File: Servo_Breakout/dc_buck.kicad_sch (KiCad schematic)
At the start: 18 parts, among them U301 BD9G500EFJ-LAE2

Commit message: finalized schematic. footprints in progress
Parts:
- C302, C305, C307, C308, C309, C310: footprint (none) -> Capacitor_SMD:C_0603_1608Metric
- C304: footprint (none) -> Capacitor_SMD:C_0603_1608Metric; now not fitted
- C306: footprint (none) -> Capacitor_THT:CP_Radial_D16.0mm_P7.50mm
- L301: footprint (none) -> Inductor_Vishay:L_Vishay_IHLP-3232
- R301, R302, R303, R305, R306, R307: footprint (none) -> Resistor_SMD:R_0603_1608Metric
- R304: footprint (none) -> Resistor_SMD:R_0603_1608Metric; now not fitted
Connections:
- net EPAD is gone; now on net GND: U301.EPAD (EXP-PAD)
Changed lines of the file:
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@@
+	(wire
+		(pts
+			(xy 180.34 91.44) (xy 180.34 95.25)
+		)
+		(stroke
+			(width 0)
+			(type default)
+		)
+	)
 	(wire
 		(pts
@@
 	(wire
 		(pts
+			(xy 69.85 90.17) (xy 82.55 90.17)
+		)
+		(stroke
+			(width 0)
+			(type default)
+		)
+	)
+	(wire
+		(pts
 			(xy 69.85 68.58) (xy 82.55 68.58)
 		)
@@
 	(wire
 		(pts
-			(xy 82.55 90.17) (xy 69.85 90.17)
-		)
-		(stroke
-			(width 0)
-			(type default)
-		)
-	)
-	(wire
-		(pts
 			(xy 194.31 97.79) (xy 194.31 100.33)
 		)
@@
 			(width 0)
 			(type default)
-		)
-	)
-	(label "EPAD"
-		(at 180.34 95.25 0)
-		(effects
-			(font
-				(size 1.27 1.27)
-			)
-			(justify left)
 		)
 	)
@@
 		)
 	)
+	(hierarchical_label "GND"
+		(shape bidirectional)
+		(at 180.34 91.44 90)
+		(effects
+			(font
+				(size 1.27 1.27)
+			)
+			(justify left)
+		)
+	)
 	(symbol
 		(lib_id "Device:R_US")
@@
 			)
 		)
-		(property "Footprint" ""
+		(property "Footprint" "Resistor_SMD:R_0603_1608Metric"
 			(at 181.356 113.284 90)
 			(effects
@@
 			)
 		)
-		(property "Footprint" ""
+		(property "Footprint" "Capacitor_SMD:C_0603_1608Metric"
 			(at 207.9752 107.95 0)
 			(effects
@@
 		(in_bom yes)
 		(on_board yes)
-		(dnp no)
+		(dnp yes)
 		(fields_autoplaced yes)
 		(property "Reference" "R304"
@@
 			)
 		)
-		(property "Footprint" ""
+		(property "Footprint" "Resistor_SMD:R_0603_1608Metric"
 			(at 120.396 75.184 90)
 			(effects
@@
 			)
 		)
-		(property "Footprint" ""
+		(property "Footprint" "Capacitor_THT:CP_Radial_D16.0mm_P7.50mm"
 			(at 70.8152 82.55 0)
 			(effects
@@
 			)
 		)
-		(property "Footprint" ""
+		(property "Footprint" "Inductor_Vishay:L_Vishay_IHLP-3232"
 			(at 99.06 68.58 0)
 			(effects
@@
 			)
 		)
-		(property "Footprint" ""
+		(property "Footprint" "Capacitor_SMD:C_0603_1608Metric"
 			(at 119.38 105.7148 0)
 			(effects
@@
 			)
 		)
-		(property "Footprint" ""
+		(property "Footprint" "Resistor_SMD:R_0603_1608Metric"
 			(at 103.124 115.824 90)
 			(effects
@@
 			)
 		)
-		(property "Footprint" ""
+		(property "Footprint" "Resistor_SMD:R_0603_1608Metric"
 			(at 161.544 67.564 90)
 			(effects
@@
 			)
 		)
-		(property "Footprint" ""
+		(property "Footprint" "Resistor_SMD:R_0603_1608Metric"
 			(at 88.646 100.584 90)
 			(effects
@@
 			)
 		)
-		(property "Footprint" ""
+		(property "Footprint" "Resistor_SMD:R_0603_1608Metric"
 			(at 103.124 105.664 90)
 			(effects
@@
 			)
 		)
-		(property "Footprint" ""
+		(property "Footprint" "Capacitor_SMD:C_0603_1608Metric"
 			(at 151.13 67.6148 0)
 			(effects
@@
 			)
 		)
-		(property "Footprint" ""
+		(property "Footprint" "Capacitor_SMD:C_0603_1608Metric"
 			(at 195.2752 107.95 0)
 			(effects
@@
 			)
 		)
-		(property "Footprint" ""
+		(property "Footprint" "Resistor_SMD:R_0603_1608Metric"
 			(at 110.744 125.984 90)
 			(effects
@@
 			)
 		)
-		(property "Footprint" ""
+		(property "Footprint" "Capacitor_SMD:C_0603_1608Metric"
 			(at 220.6752 107.95 0)
 			(effects
@@
 		(in_bom yes)
 		(on_board yes)
-		(dnp no)
+		(dnp yes)
 		(fields_autoplaced yes)
 		(property "Reference" "C304"
@@
 			)
 		)
-		(property "Footprint" ""
+		(property "Footprint" "Capacitor_SMD:C_0603_1608Metric"
 			(at 120.3452 88.9 0)
 			(effects
@@
 			)
 		)
-		(property "Footprint" ""
+		(property "Footprint" "Capacitor_SMD:C_0603_1608Metric"
 			(at 83.5152 82.55 0)
 			(effects

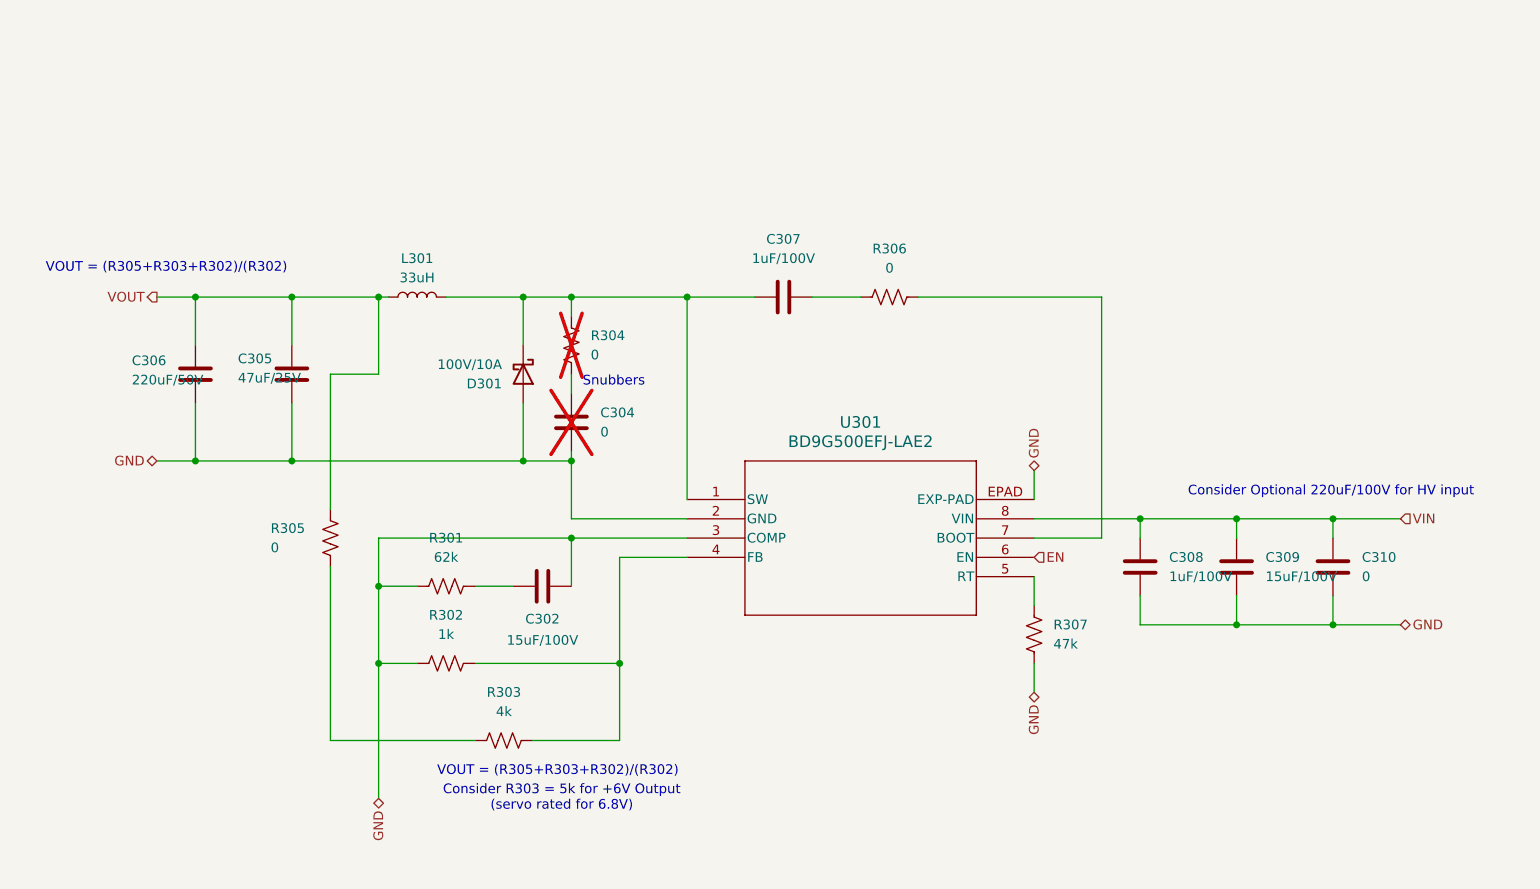
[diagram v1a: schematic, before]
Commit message: replaced Micro with 555 Timer for PWM generation. completed most of layout
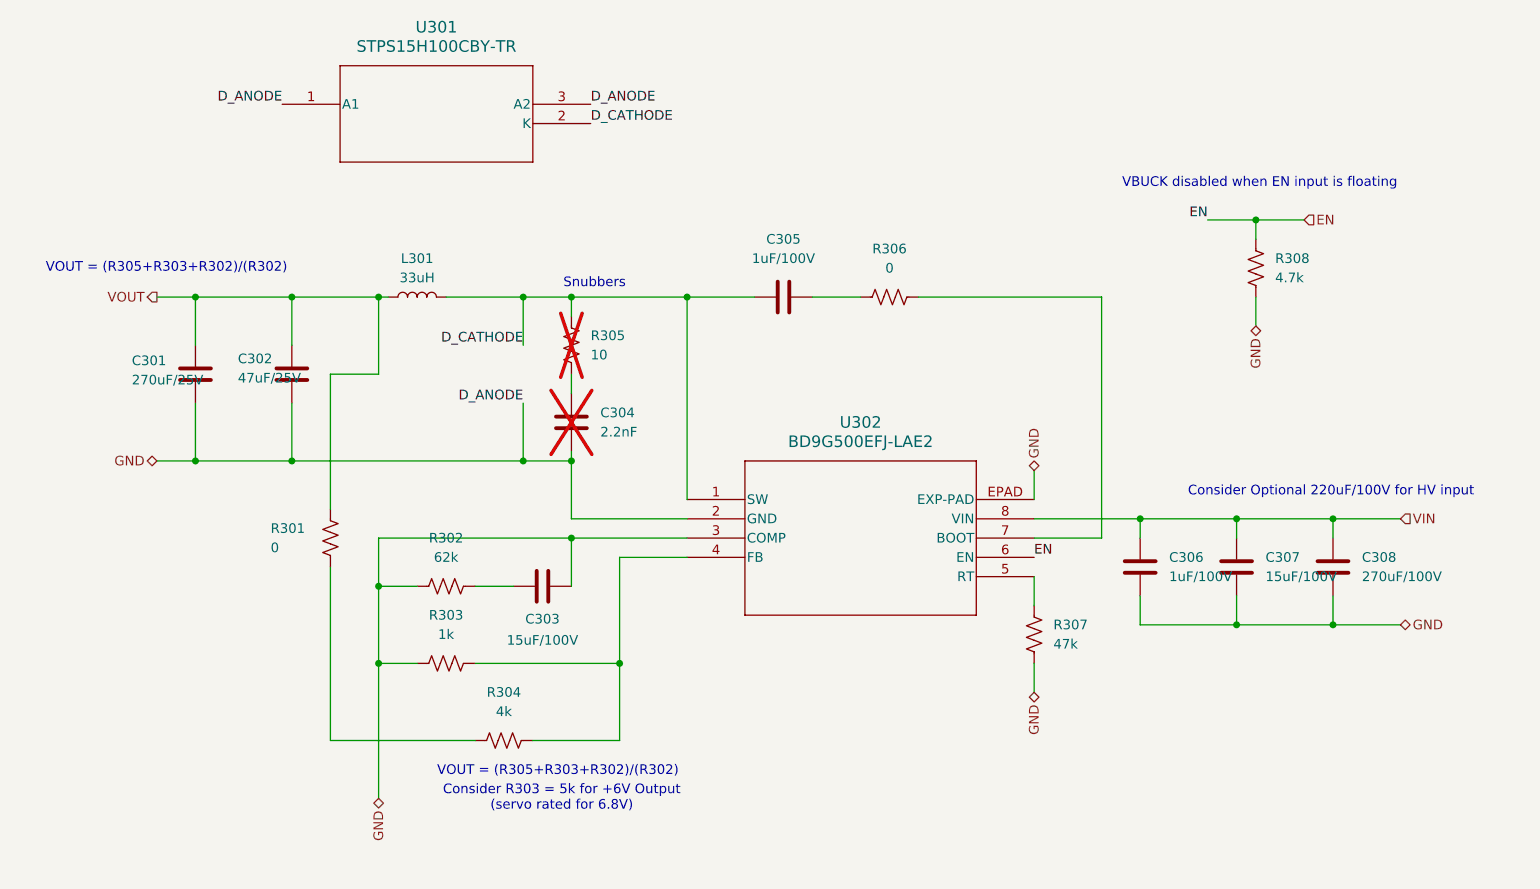
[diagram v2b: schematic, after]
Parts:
- removed D301: 100V/10A, symbol Device:D_Schottky
- added R308: 4.7k, Resistor_SMD:R_0805_2012Metric_Pad1.20x1.40mm_HandSolder, symbol Device:R_US
- added U301: STPS15H100CBY-TR, STPS15H100CBY-TR:STPS15H100CBY-TR, symbol STPS15H100CBY-TR:STPS15H100CBY-TR
- C301: renamed from C306; value 220uF/50V -> 270uF/25V; footprint Capacitor_THT:CP_Radial_D16.0mm_P7.50mm -> Capacitor_THT:CP_Radial_D10.0mm_P5.00mm
- C302: renamed from C305; footprint Capacitor_SMD:C_0603_1608Metric -> Capacitor_SMD:C_2220_5750Metric_Pad1.97x5.40mm_HandSolder
- C303: renamed from C302; footprint Capacitor_SMD:C_0603_1608Metric -> Capacitor_SMD:C_2220_5750Metric_Pad1.97x5.40mm_HandSolder
- C304: value 0 -> 2.2nF; footprint Capacitor_SMD:C_0603_1608Metric -> Capacitor_SMD:C_0805_2012Metric_Pad1.18x1.45mm_HandSolder
- C305: renamed from C307; footprint Capacitor_SMD:C_0603_1608Metric -> Capacitor_SMD:C_0805_2012Metric_Pad1.18x1.45mm_HandSolder
- C306: renamed from C308; footprint Capacitor_SMD:C_0603_1608Metric -> Capacitor_SMD:C_0805_2012Metric_Pad1.18x1.45mm_HandSolder
- C307: renamed from C309; footprint Capacitor_SMD:C_0603_1608Metric -> Capacitor_SMD:C_2220_5750Metric_Pad1.97x5.40mm_HandSolder
- C308: renamed from C310; value 0 -> 270uF/100V; footprint Capacitor_SMD:C_0603_1608Metric -> Capacitor_THT:CP_Radial_D16.0mm_P7.50mm
- R301: renamed from R305; footprint Resistor_SMD:R_0603_1608Metric -> Resistor_SMD:R_0805_2012Metric_Pad1.20x1.40mm_HandSolder
- R302: renamed from R301; footprint Resistor_SMD:R_0603_1608Metric -> Resistor_SMD:R_0805_2012Metric_Pad1.20x1.40mm_HandSolder
- R303: renamed from R302; footprint Resistor_SMD:R_0603_1608Metric -> Resistor_SMD:R_0805_2012Metric_Pad1.20x1.40mm_HandSolder
- R304: renamed from R303; footprint Resistor_SMD:R_0603_1608Metric -> Resistor_SMD:R_0805_2012Metric_Pad1.20x1.40mm_HandSolder
- R305: renamed from R304; value 0 -> 10; footprint Resistor_SMD:R_0603_1608Metric -> Resistor_SMD:R_0805_2012Metric_Pad1.20x1.40mm_HandSolder
- R306, R307: footprint Resistor_SMD:R_0603_1608Metric -> Resistor_SMD:R_0805_2012Metric_Pad1.20x1.40mm_HandSolder
- U302: renamed from U301; footprint SOIC8_BD9G500EFJ-LAE2_ROM -> BD9G500EFJ:SOIC8_BD9G500EFJ-LAE2_ROM
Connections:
- net EN: now also R308.2
- net GND: now also R308.1, U301.1 (A1), U301.3 (A2)
- net D_CATHODE: now reaches C305.1, L301.2, R305.1, U302.1 (SW)
- net D_CATHODE: now also U301.2 (K)
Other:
- note added: "VBUCK disabled when EN input is floating"

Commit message: fixed deprecaited VOUT comments
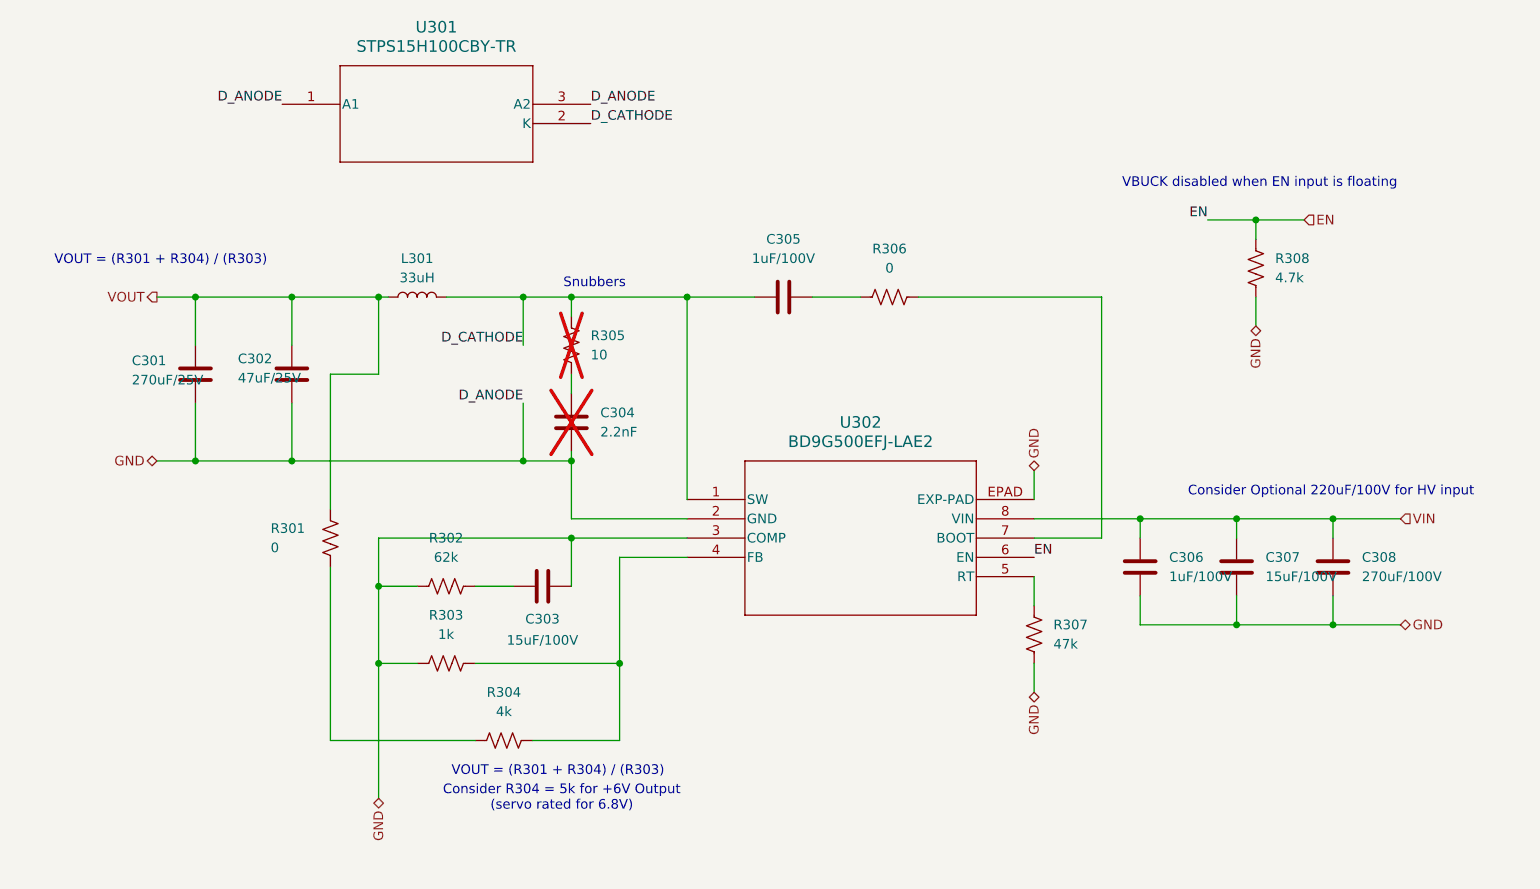
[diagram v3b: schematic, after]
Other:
- note added: "Consider R304 = 5k for +6V Output (servo rated for 6.8V)"
- note added: "VOUT = (R301 + R304) / (R303)"
- note removed: "Consider R303 = 5k for +6V Output (servo rated for 6.8V)"
- note removed: "VOUT = (R305+R303+R302)/(R302)"
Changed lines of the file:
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@@
 		)
 	)
-	(text "VOUT = (R305+R303+R302)/(R302)"
+	(text "VOUT = (R301 + R304) / (R303)"
 		(exclude_from_sim no)
-		(at 66.04 64.77 0)
+		(at 65.278 63.754 0)
 		(effects
 			(font
@@
 		)
 	)
-	(text "Consider R303 = 5k for +6V Output\n(servo rated for 6.8V)"
+	(text "Consider R304 = 5k for +6V Output\n(servo rated for 6.8V)"
 		(exclude_from_sim no)
 		(at 118.11 134.62 0)
@@
 		)
 	)
-	(text "VOUT = (R305+R303+R302)/(R302)"
+	(text "VOUT = (R301 + R304) / (R303)"
 		(exclude_from_sim no)
 		(at 117.602 131.064 0)
